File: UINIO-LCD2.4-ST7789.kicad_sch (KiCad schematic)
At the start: 35 parts, among them CON1 FFC_8Pin_0.5mm, J1 Conn_01x08_Male, Q1 S8050, U1 ME6211C33M5G-N, U2 AMS1117, U3 XC6206P332MR, U4 CON_10Pin

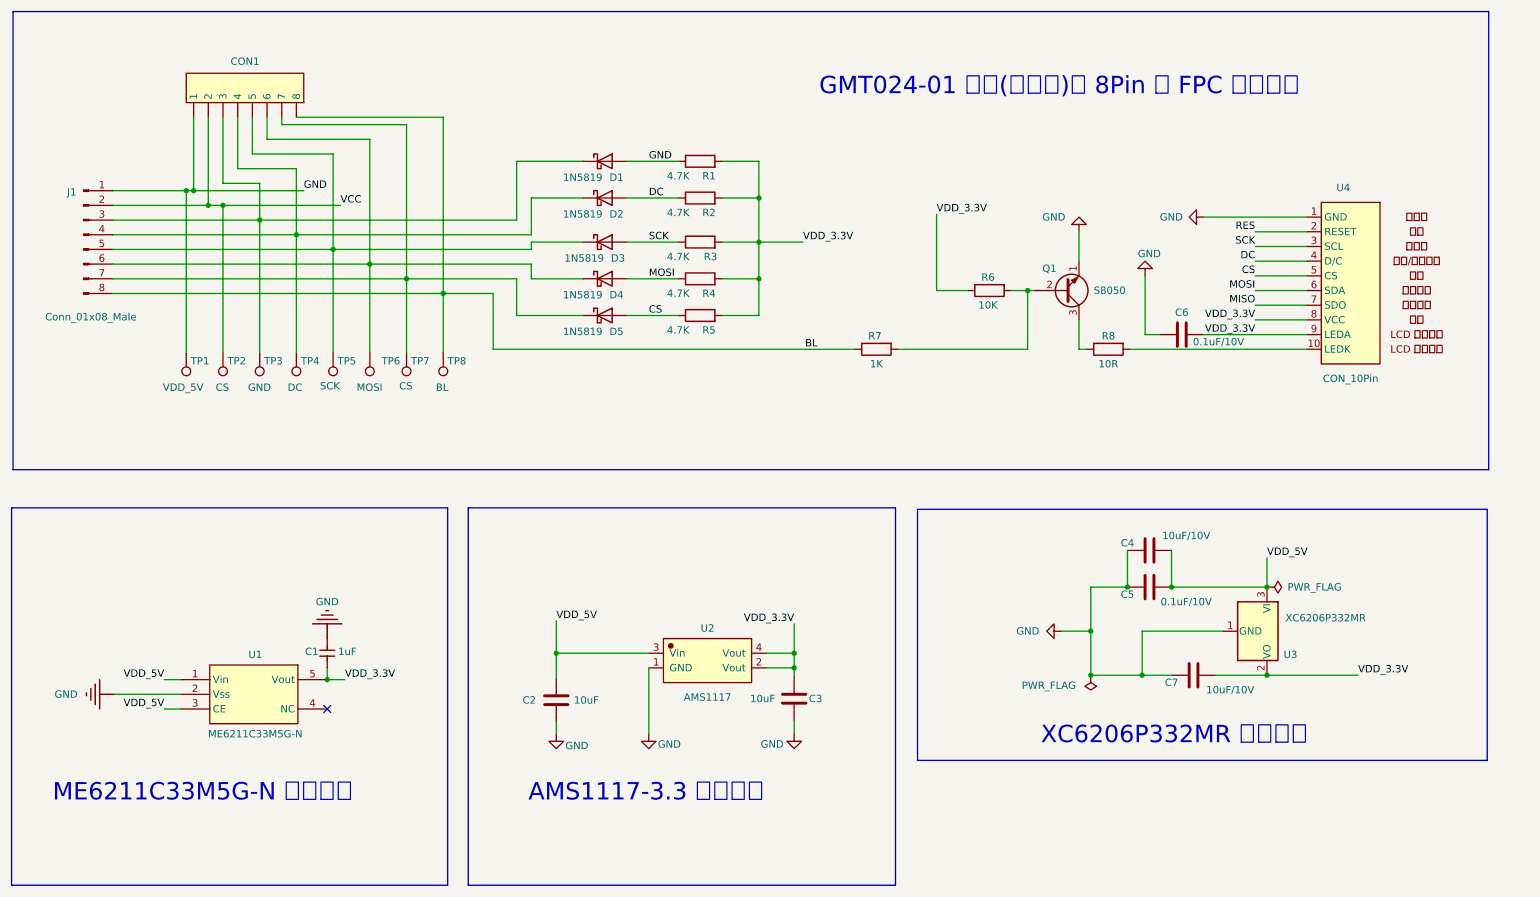
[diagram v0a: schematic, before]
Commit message: redistributed chip packaging.
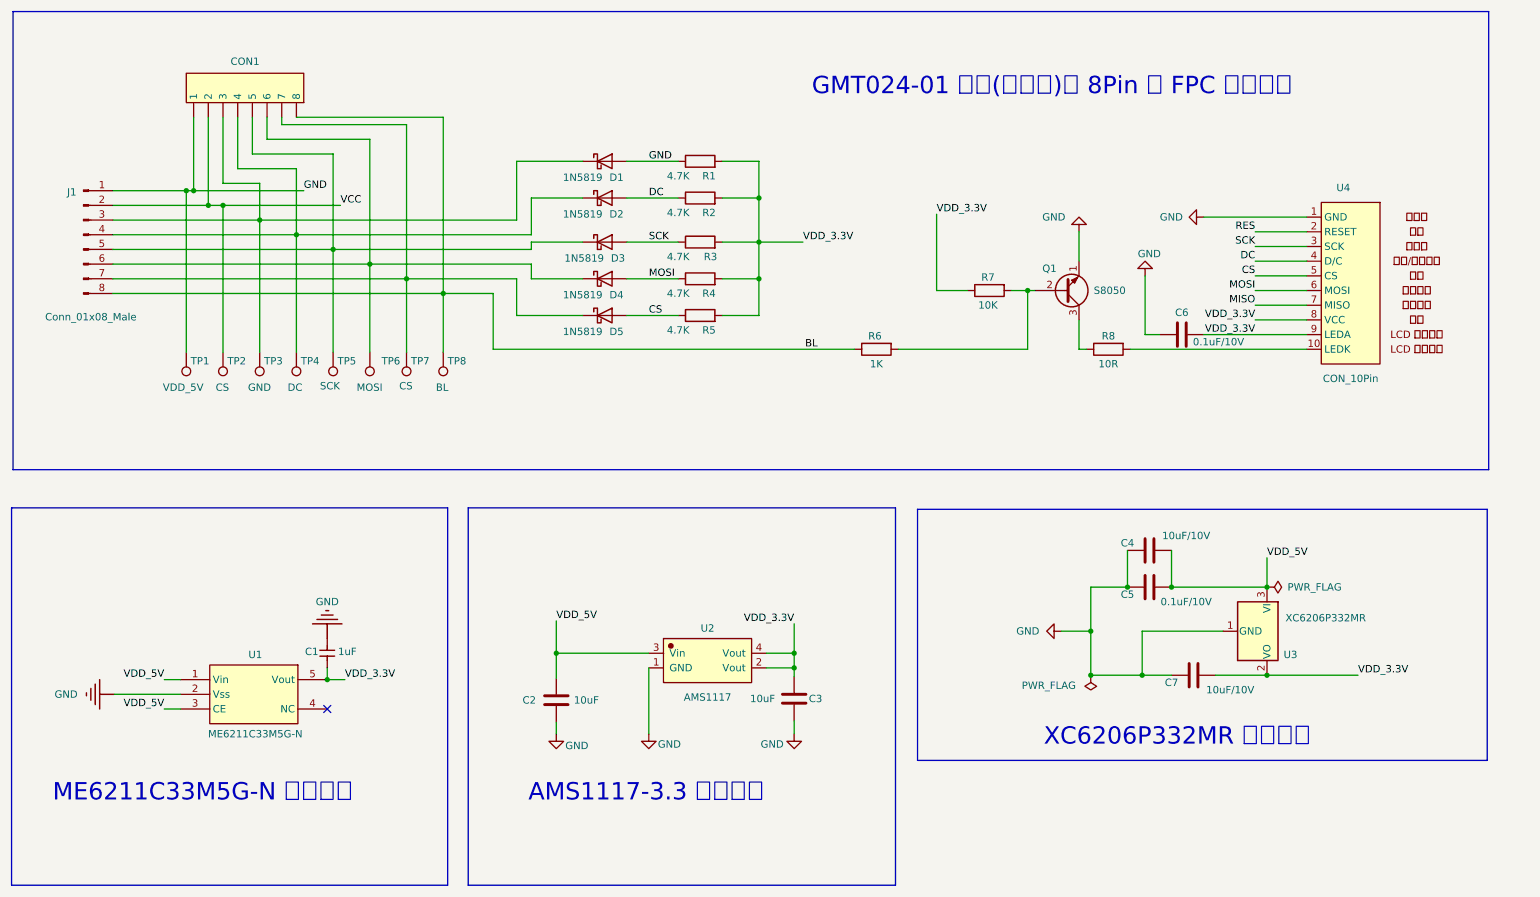
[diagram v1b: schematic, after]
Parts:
- C1: footprint Capacitor_SMD:C_0402_1005Metric -> Uinio:CAP_0402
- C4, C5, C6, C7: footprint (none) -> Capacitor_SMD:C_0603_1608Metric
- J1: footprint (none) -> Connector_PinHeader_2.54mm:PinHeader_1x08_P2.54mm_Vertical
- R1, R2, R3, R4, R5, R8: footprint (none) -> Resistor_SMD:R_0603_1608Metric
- R6: renamed from R7; footprint (none) -> Resistor_SMD:R_0603_1608Metric
- R7: renamed from R6; footprint (none) -> Resistor_SMD:R_0603_1608Metric
- TP1, TP2, TP3, TP4, TP5, TP6, TP7, TP8: footprint (none) -> TestPoint:TestPoint_Pad_D2.0mm
- U1: footprint Uinio:SOT-23-5_L3.0-W1.7-P0.95-LS2.8-BR -> Uinio:SOT23-5
- U2: footprint Uinio:SOT-223-4_L6.5-W3.5-P2.30-LS7.0-BR -> kicad_lceda:SOT-223-3_L6.6-W3.5-P2.30-LS7.0-BL
- U4: footprint (none) -> Uinio:LCD-ST7789-10Pin

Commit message: update packaging.
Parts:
- C1: footprint Uinio:CAP_0402 -> Capacitor_SMD:C_0603_1608Metric
- C2, C3: footprint Capacitor_SMD:C_0402_1005Metric -> Capacitor_SMD:C_0603_1608Metric
- D1, D2, D3, D4, D5: footprint Diode_THT:D_DO-41_SOD81_P10.16mm_Horizontal -> Uinio:SOD-123_L2.7-W1.6-LS3.7-RD-1
- Q1: footprint Package_TO_SOT_THT:TO-92_Inline -> Uinio:SOT-23-3_L2.9-W1.6-P1.90-LS2.9-BL
- U1: footprint Uinio:SOT23-5 -> Uinio:SOT-23-5_L3.0-W1.7-P0.95-LS2.8-BR
- U2: footprint kicad_lceda:SOT-223-3_L6.6-W3.5-P2.30-LS7.0-BL -> Uinio:SOT-223-3_L6.6-W3.5-P2.30-LS7.0-BL
- U3: footprint Package_TO_SOT_SMD:SOT-23 -> Uinio:SOT-23-3_L2.9-W1.6-P1.90-LS2.9-BL
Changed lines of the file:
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@@
     (property "Reference" "D3" (id 0) (at 125.222 74.676 0))
     (property "Value" "1N5819" (id 1) (at 119.38 74.676 0))
-    (property "Footprint" "Diode_THT:D_DO-41_SOD81_P10.16mm_Horizontal" (id 2) (at 122.936 76.327 0)
+    (property "Footprint" "Uinio:SOD-123_L2.7-W1.6-LS3.7-RD-1" (id 2) (at 122.936 76.327 0)
       (effects (font (size 1.27 1.27)) hide)
     )
@@
     (property "Reference" "U2" (id 0) (at 140.716 138.684 0))
     (property "Value" "AMS1117" (id 1) (at 140.716 150.622 0))
-    (property "Footprint" "kicad_lceda:SOT-223-3_L6.6-W3.5-P2.30-LS7.0-BL" (id 2) (at 140.716 142.875 0)
+    (property "Footprint" "Uinio:SOT-223-3_L6.6-W3.5-P2.30-LS7.0-BL" (id 2) (at 140.716 142.875 0)
       (effects (font (size 1.27 1.27)) hide)
     )
@@
     (property "Reference" "D1" (id 0) (at 124.968 60.706 0))
     (property "Value" "1N5819" (id 1) (at 119.126 60.706 0))
-    (property "Footprint" "Diode_THT:D_DO-41_SOD81_P10.16mm_Horizontal" (id 2) (at 122.936 62.357 0)
+    (property "Footprint" "Uinio:SOD-123_L2.7-W1.6-LS3.7-RD-1" (id 2) (at 122.936 62.357 0)
       (effects (font (size 1.27 1.27)) hide)
     )
@@
     (property "Reference" "D2" (id 0) (at 124.968 67.056 0))
     (property "Value" "1N5819" (id 1) (at 119.126 67.056 0))
-    (property "Footprint" "Diode_THT:D_DO-41_SOD81_P10.16mm_Horizontal" (id 2) (at 122.936 68.707 0)
+    (property "Footprint" "Uinio:SOD-123_L2.7-W1.6-LS3.7-RD-1" (id 2) (at 122.936 68.707 0)
       (effects (font (size 1.27 1.27)) hide)
     )
@@
       (effects (font (size 1.27 1.27)) (justify left))
     )
-    (property "Footprint" "Capacitor_SMD:C_0402_1005Metric" (id 2) (at 115.5192 154.94 0)
+    (property "Footprint" "Capacitor_SMD:C_0603_1608Metric" (id 2) (at 115.5192 154.94 0)
       (effects (font (size 1.27 1.27)) hide)
     )
@@
       (effects (font (size 1.27 1.27)) (justify left))
     )
-    (property "Footprint" "Package_TO_SOT_THT:TO-92_Inline" (id 2) (at 207.518 78.359 0)
+    (property "Footprint" "Uinio:SOT-23-3_L2.9-W1.6-P1.90-LS2.9-BL" (id 2) (at 207.518 78.359 0)
       (effects (font (size 1.27 1.27) italic) (justify left) hide)
     )
@@
     (property "Reference" "U1" (id 0) (at 62.484 143.256 0))
     (property "Value" "ME6211C33M5G-N" (id 1) (at 62.484 156.972 0))
-    (property "Footprint" "Uinio:SOT23-5" (id 2) (at 49.53 147.574 0)
+    (property "Footprint" "Uinio:SOT-23-5_L3.0-W1.7-P0.95-LS2.8-BR" (id 2) (at 49.53 147.574 0)
       (effects (font (size 1.27 1.27)) hide)
     )
@@
       (effects (font (size 1.27 1.27)) (justify left bottom))
     )
-    (property "Footprint" "Uinio:CAP_0402" (id 2) (at 74.93 143.002 0)
+    (property "Footprint" "Capacitor_SMD:C_0603_1608Metric" (id 2) (at 74.93 143.002 0)
       (effects (font (size 1.27 1.27)) hide)
     )
@@
       (effects (font (size 1.27 1.27)) (justify left))
     )
-    (property "Footprint" "Capacitor_SMD:C_0402_1005Metric" (id 2) (at 156.6672 154.686 0)
+    (property "Footprint" "Capacitor_SMD:C_0603_1608Metric" (id 2) (at 156.6672 154.686 0)
       (effects (font (size 1.27 1.27)) hide)
     )
@@
     (property "Reference" "D5" (id 0) (at 124.968 87.376 0))
     (property "Value" "1N5819" (id 1) (at 119.126 87.376 0))
-    (property "Footprint" "Diode_THT:D_DO-41_SOD81_P10.16mm_Horizontal" (id 2) (at 122.936 89.027 0)
+    (property "Footprint" "Uinio:SOD-123_L2.7-W1.6-LS3.7-RD-1" (id 2) (at 122.936 89.027 0)
       (effects (font (size 1.27 1.27)) hide)
     )
@@
     (property "Reference" "U3" (id 0) (at 241.554 143.256 90))
     (property "Value" "XC6206P332MR" (id 1) (at 247.65 136.906 90))
-    (property "Footprint" "Package_TO_SOT_SMD:SOT-23" (id 2) (at 243.205 139.192 0)
+    (property "Footprint" "Uinio:SOT-23-3_L2.9-W1.6-P1.90-LS2.9-BL" (id 2) (at 243.205 139.192 0)
       (effects (font (size 1.27 1.27) italic) hide)
     )
@@
     (property "Reference" "D4" (id 0) (at 124.968 81.026 0))
     (property "Value" "1N5819" (id 1) (at 119.126 81.026 0))
-    (property "Footprint" "Diode_THT:D_DO-41_SOD81_P10.16mm_Horizontal" (id 2) (at 122.936 82.677 0)
+    (property "Footprint" "Uinio:SOD-123_L2.7-W1.6-LS3.7-RD-1" (id 2) (at 122.936 82.677 0)
       (effects (font (size 1.27 1.27)) hide)
     )
@@
     )
     (path "/d6f5fccc-0486-41e9-aa20-ea594a3fd246"
-      (reference "C1") (unit 1) (value "1uF") (footprint "Uinio:CAP_0402")
+      (reference "C1") (unit 1) (value "1uF") (footprint "Capacitor_SMD:C_0603_1608Metric")
     )
     (path "/43474df2-e753-4366-971d-f71f4ac1b244"
-      (reference "C2") (unit 1) (value "10uF") (footprint "Capacitor_SMD:C_0402_1005Metric")
+      (reference "C2") (unit 1) (value "10uF") (footprint "Capacitor_SMD:C_0603_1608Metric")
     )
     (path "/eef5cd36-83dc-46cf-bdcb-a2779f7bbdcc"
-      (reference "C3") (unit 1) (value "10uF") (footprint "Capacitor_SMD:C_0402_1005Metric")
+      (reference "C3") (unit 1) (value "10uF") (footprint "Capacitor_SMD:C_0603_1608Metric")
     )
     (path "/39db6470-d19f-4778-a169-c2772d085c20"
@@
     )
     (path "/367c4f33-761a-407c-b60f-f5f20f0d0163"
-      (reference "D1") (unit 1) (value "1N5819") (footprint "Diode_THT:D_DO-41_SOD81_P10.16mm_Horizontal")
+      (reference "D1") (unit 1) (value "1N5819") (footprint "Uinio:SOD-123_L2.7-W1.6-LS3.7-RD-1")
     )
     (path "/3c397e15-1f91-4497-842d-d7eaa0b7fa75"
-      (reference "D2") (unit 1) (value "1N5819") (footprint "Diode_THT:D_DO-41_SOD81_P10.16mm_Horizontal")
+      (reference "D2") (unit 1) (value "1N5819") (footprint "Uinio:SOD-123_L2.7-W1.6-LS3.7-RD-1")
     )
     (path "/00010048-5843-419b-b601-b0b32814b7a9"
-      (reference "D3") (unit 1) (value "1N5819") (footprint "Diode_THT:D_DO-41_SOD81_P10.16mm_Horizontal")
+      (reference "D3") (unit 1) (value "1N5819") (footprint "Uinio:SOD-123_L2.7-W1.6-LS3.7-RD-1")
     )
     (path "/fbbaf3e0-1544-4e0d-8ef0-6baf021c5a53"
-      (reference "D4") (unit 1) (value "1N5819") (footprint "Diode_THT:D_DO-41_SOD81_P10.16mm_Horizontal")
+      (reference "D4") (unit 1) (value "1N5819") (footprint "Uinio:SOD-123_L2.7-W1.6-LS3.7-RD-1")
     )
     (path "/f4a26868-ce4a-4a50-91cc-8c24c9a2ba4f"
-      (reference "D5") (unit 1) (value "1N5819") (footprint "Diode_THT:D_DO-41_SOD81_P10.16mm_Horizontal")
+      (reference "D5") (unit 1) (value "1N5819") (footprint "Uinio:SOD-123_L2.7-W1.6-LS3.7-RD-1")
     )
     (path "/e0933afa-aea0-4851-b0ee-a71d4d0af181"
@@
     )
     (path "/98322e5e-9958-45f2-b44f-977945bfe5ca"
-      (reference "Q1") (unit 1) (value "S8050") (footprint "Package_TO_SOT_THT:TO-92_Inline")
+      (reference "Q1") (unit 1) (value "S8050") (footprint "Uinio:SOT-23-3_L2.9-W1.6-P1.90-LS2.9-BL")
     )
     (path "/718b7be7-aaec-4241-9886-b09d047d4206"
@@
     )
     (path "/a8957b38-5f25-4171-9553-5534326af44e"
-      (reference "U1") (unit 1) (value "ME6211C33M5G-N") (footprint "Uinio:SOT23-5")
+      (reference "U1") (unit 1) (value "ME6211C33M5G-N") (footprint "Uinio:SOT-23-5_L3.0-W1.7-P0.95-LS2.8-BR")
     )
     (path "/2f1c364a-de62-481f-84f4-2b52a179abbc"
-      (reference "U2") (unit 1) (value "AMS1117") (footprint "kicad_lceda:SOT-223-3_L6.6-W3.5-P2.30-LS7.0-BL")
+      (reference "U2") (unit 1) (value "AMS1117") (footprint "Uinio:SOT-223-3_L6.6-W3.5-P2.30-LS7.0-BL")
     )
     (path "/f4b08de0-cafa-49df-be17-3aa6f9f346a4"
-      (reference "U3") (unit 1) (value "XC6206P332MR") (footprint "Package_TO_SOT_SMD:SOT-23")
+      (reference "U3") (unit 1) (value "XC6206P332MR") (footprint "Uinio:SOT-23-3_L2.9-W1.6-P1.90-LS2.9-BL")
     )
     (path "/ceeac562-3738-4b6c-a1ba-215e2cd9e3b4"

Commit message: start drawing PCB.
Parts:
- TP2: value CS -> GND
- TP3: value GND -> CS
- TP7: value CS -> RES
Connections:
- net CS: now also D1.2 (A), R1.1; no longer D5.2 (A), R5.1
- net GND: now also CON1.3, J1.3 (Pin_3), TP3.1; no longer CON1.1, D1.2 (A), J1.1 (Pin_1), R1.1, TP1.1
- net RES: now also D5.2 (A), R5.1
- net VDD_5V: now also CON1.1, J1.1 (Pin_1), TP1.1
- net VCC: no longer names the net of CON1.2, J1.2 (Pin_2), TP2.1
- net VCC: now also D1.1 (K)

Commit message: finish layout.
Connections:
- no-connect marks 1 -> 2
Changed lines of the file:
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@@
   )
   (no_connect (at 74.93 152.654))
+  (no_connect (at 235.458 82.804))
   (wire (pts (xy 196.088 80.264) (xy 197.358 80.264))
     (stroke (width 0) (type default) (color 0 0 0 0))
